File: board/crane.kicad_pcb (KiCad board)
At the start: 4 copper layers, 71 x 226 mm, 79 parts, among them IC1 PMV48XP, J1 USB-B-S-X-X-TH, J10 AVR-ISP-6, J8 AVR-ISP-6, SW1 SW_Push, SW10 SW_Push, SW11 SW_Push, SW12 SW_Push, SW2 SW_Push, SW3 SW_Push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

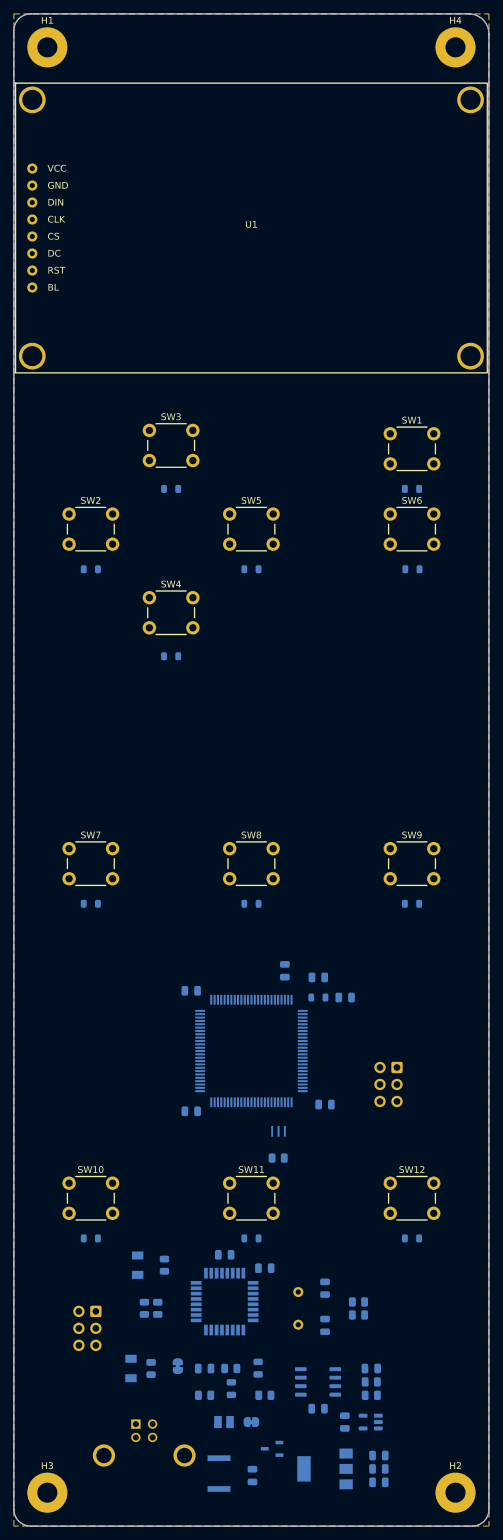
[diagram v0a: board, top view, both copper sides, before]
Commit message: Completed routing
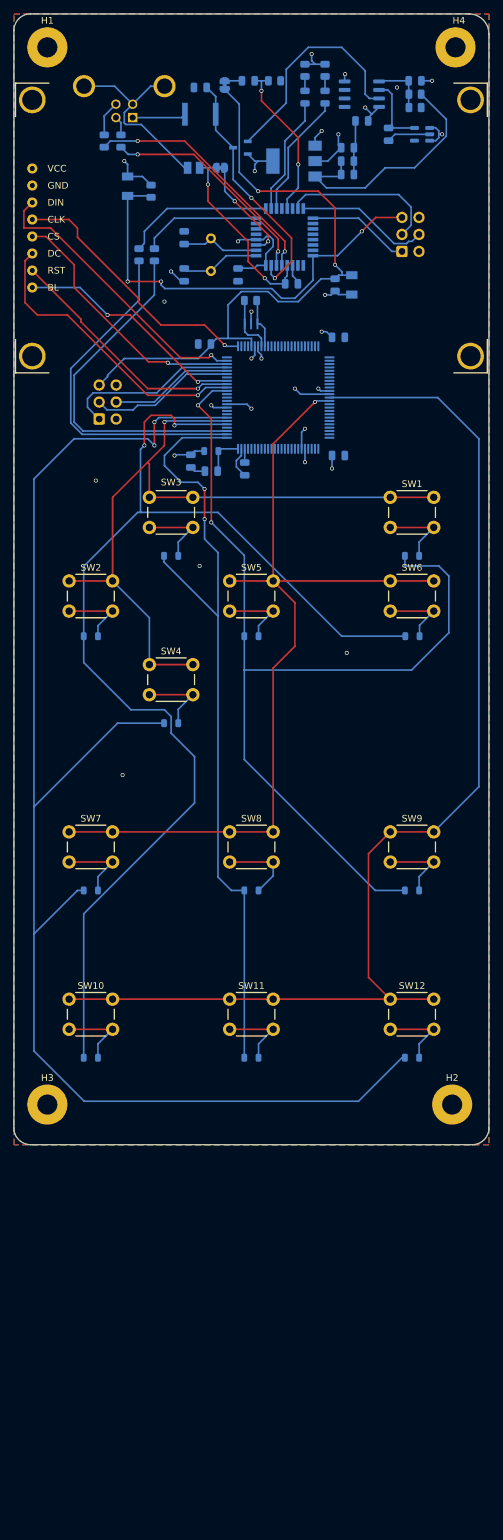
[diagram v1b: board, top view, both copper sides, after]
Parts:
- moved C13 207.6 mm to (142.4, 98.0), turned to 180 degrees
- moved J1 204.7 mm to (131.0, 97.8), turned to 0 degrees
- moved F1 203.2 mm to (142.4, 102.0), turned to 0 degrees
- moved R12 198.8 mm to (161.0, 95.4), turned to 90 degrees
- moved R11 198.1 mm to (158.0, 95.4), turned to 90 degrees
- moved C10 195.5 mm to (164.4, 107.0)
- moved C8 195.5 mm to (164.4, 111.0)
- moved C9 195.5 mm to (164.4, 109.0)
- moved U4 195.5 mm to (156.4, 109.0)
- moved IC1 194.5 mm to (148.4, 107.0)
- moved D16 193.5 mm to (161.0, 99.4), turned to 90 degrees
- moved U5 192.6 mm to (175.5, 105.0)
- moved C1 192.6 mm to (166.5, 103.0)
- moved C12 192.6 mm to (170.5, 105.0)
- moved C18 192.6 mm to (149.5, 97.0)
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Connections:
- net Net-(F1-Pad1) renamed /MCU/USBVCC_SOCKET
- net Net-(J1-Pad2) renamed /MCU/USB_D-
- net Net-(J1-Pad3) renamed /MCU/USB_D+
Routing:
- net SW_R3: track 0.00 -> 217.0 mm, vias 0 -> 2
- net SW_R1: track 0.00 -> 176.9 mm, vias 0 -> 2
- net SW_C2: track 0.00 -> 175.1 mm
- net SW_R0: track 0.00 -> 143.2 mm, vias 0 -> 2
- net SW_C1: track 0.00 -> 132.8 mm, vias 0 -> 1
- net SW_R2: track 0.00 -> 120.3 mm, vias 0 -> 2
- net SW_C0: track 0.00 -> 112.0 mm, vias 0 -> 1
- net RESET: track 0.00 -> 94.0 mm, vias 0 -> 2
- net +5V: track 0.00 -> 68.6 mm, vias 0 -> 15
- net RESET2: track 0.00 -> 65.9 mm, vias 0 -> 3
- net RX0: track 0.00 -> 52.5 mm
- net TX0: track 0.00 -> 52.4 mm
- net GND: track 0.00 -> 46.2 mm, vias 0 -> 15
- net LCD_DC: track 0.00 -> 44.2 mm, vias 0 -> 1
- net LCD_DIN: track 0.00 -> 43.2 mm, vias 0 -> 1
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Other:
- board size 71 x 226 mm -> 71 x 169 mm

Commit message: Added Mizzan Logo
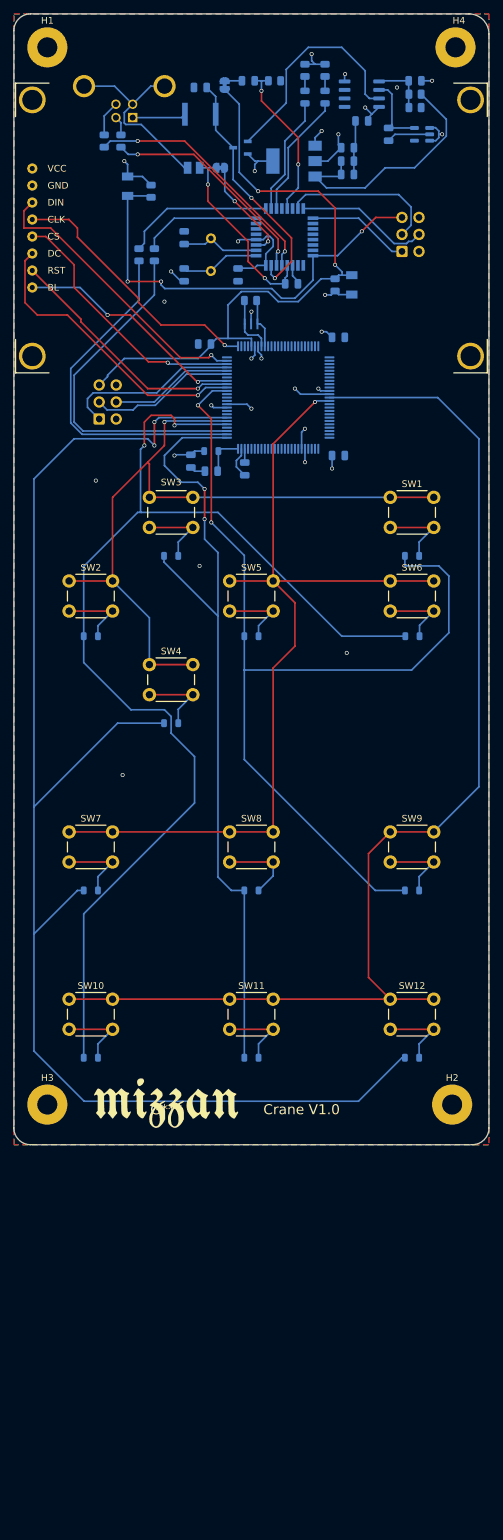
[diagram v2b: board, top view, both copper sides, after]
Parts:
- added G***: LOGO, footprints:mizzan_logo, F.Cu at (137.2, 250.8)
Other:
- board text added: "Crane V1.0"
